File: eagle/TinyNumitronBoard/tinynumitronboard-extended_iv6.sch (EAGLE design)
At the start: 35 parts

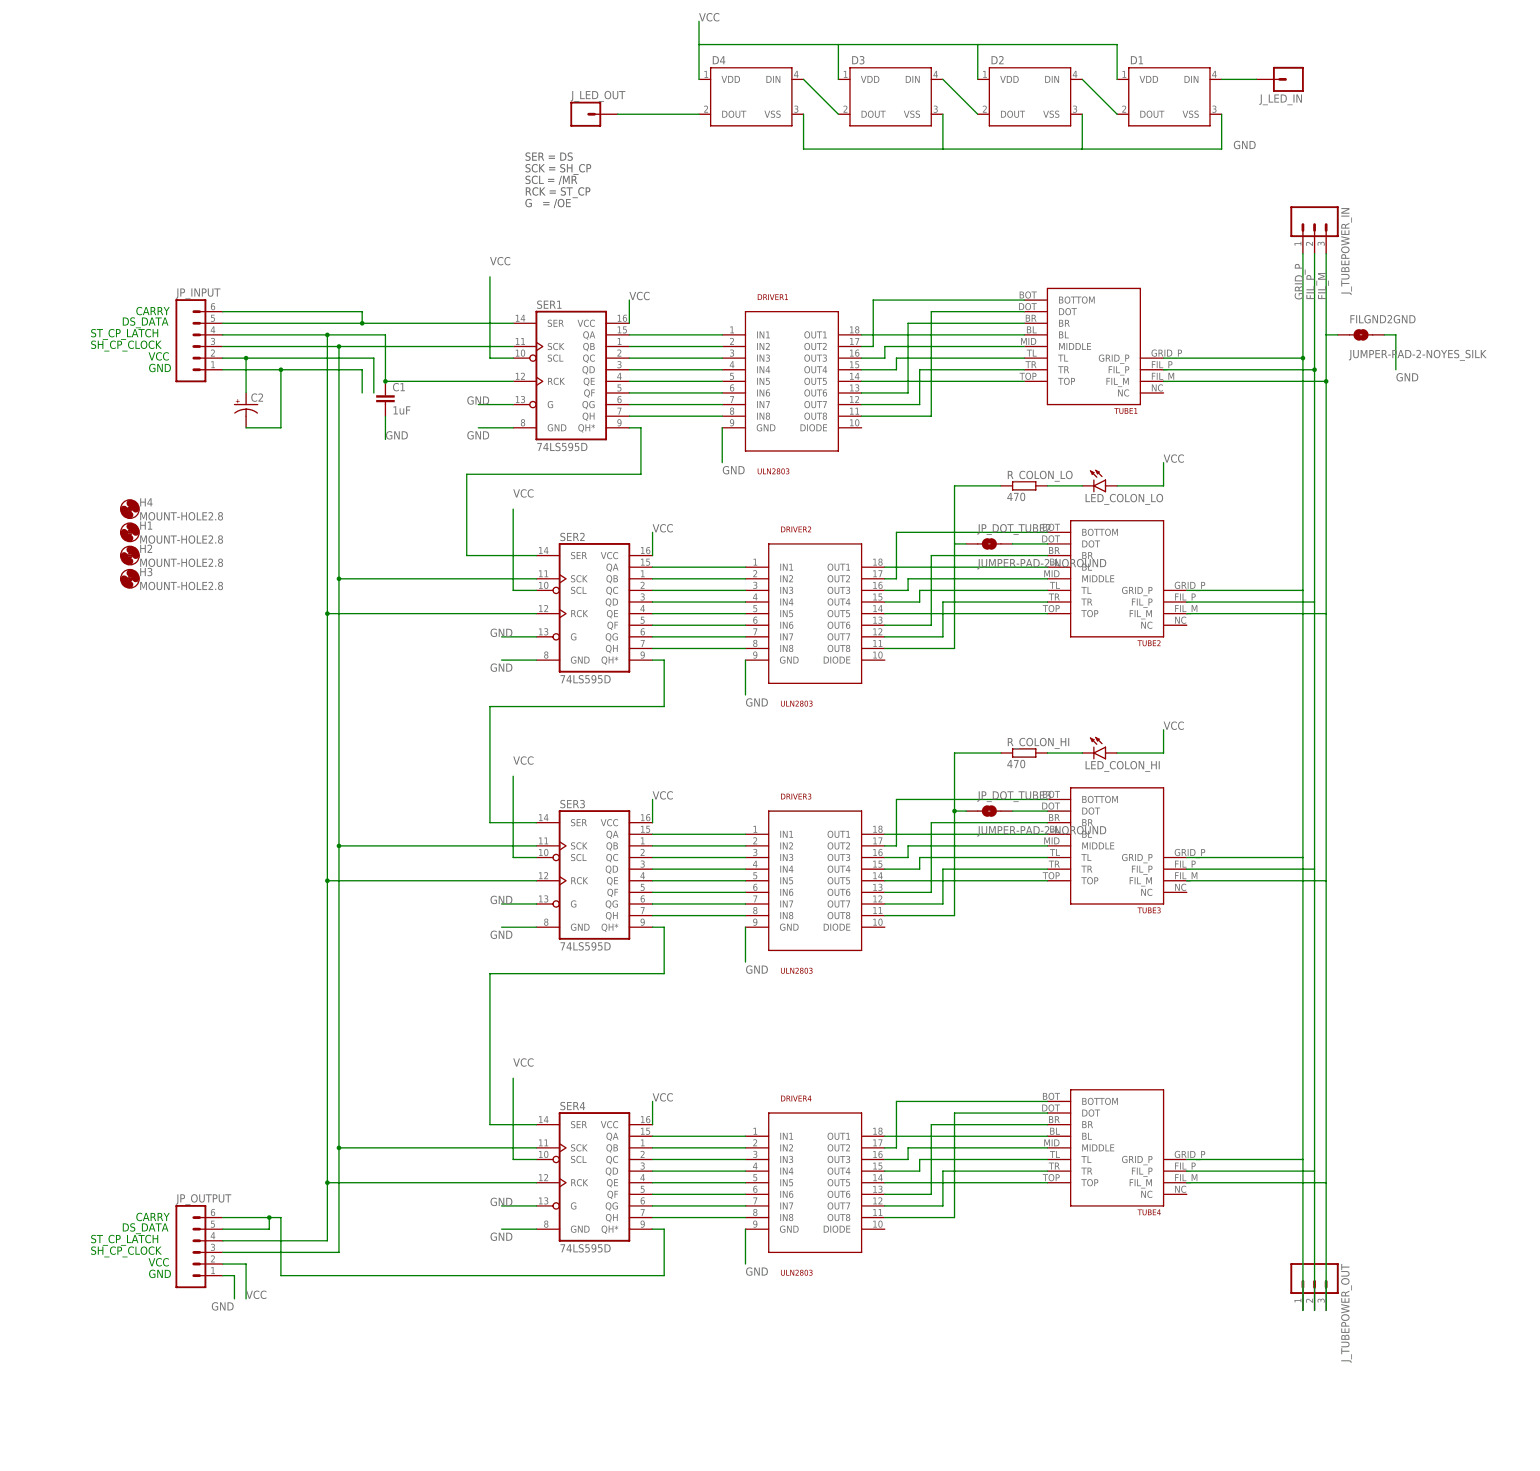
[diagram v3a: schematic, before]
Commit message: added pad for UL2803 diode/common
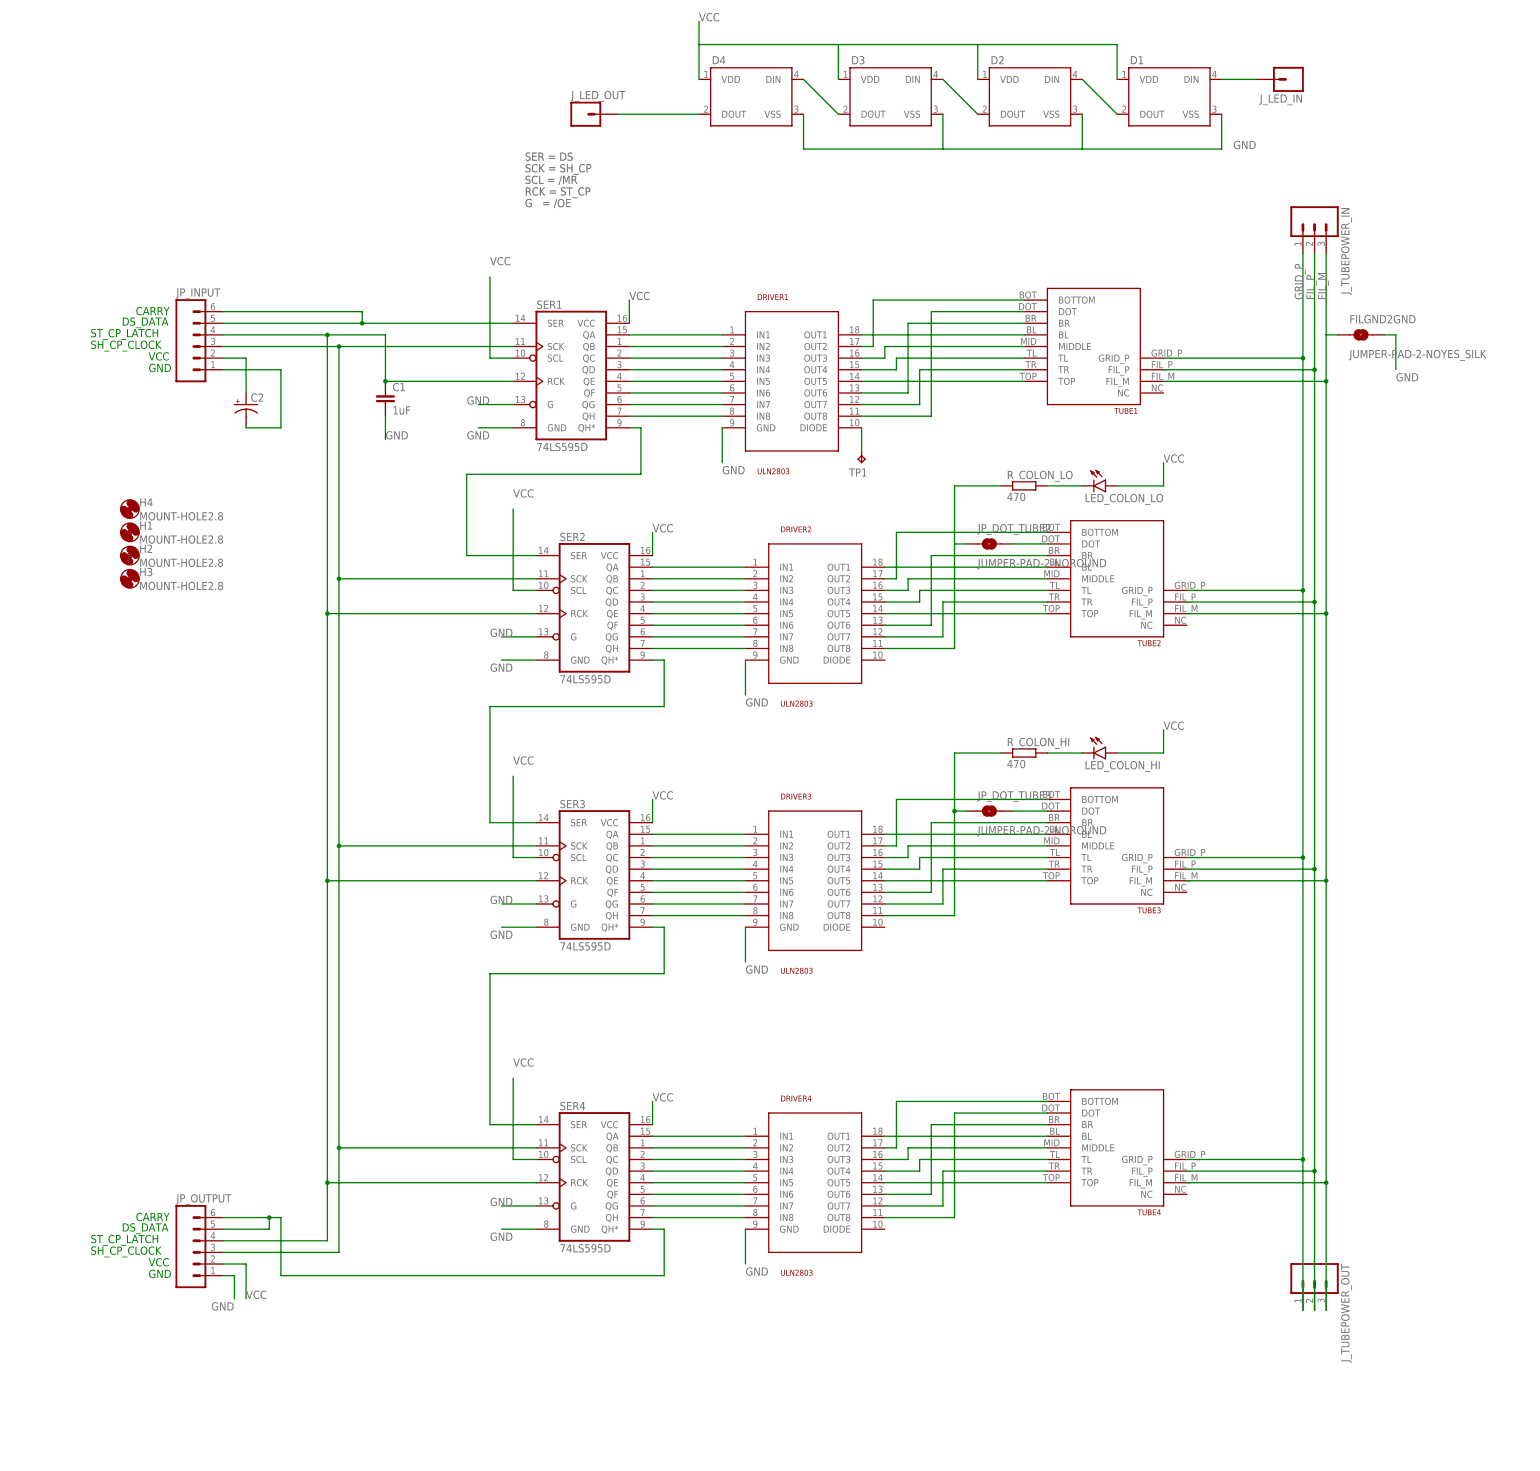
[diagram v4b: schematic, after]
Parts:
- added TP1: TPB2,54, testpad:TPB2,54
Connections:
- new net DIODE: DRIVER1.DIODE, TP1.TP
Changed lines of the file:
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@@
 <part name="R_COLON_HI" library="resistor" deviceset="R-EU_" device="M1206" value="470"/>
 <part name="JP_DOT_TUBE3" library="SparkFun-Passives" deviceset="JUMPER-PAD-2-NO" device="ROUND"/>
+<part name="TP1" library="testpad" deviceset="TP" device="B2,54" value="TPB2,54"/>
 </parts>
 <sheets>
@@
 <instance part="R_COLON_HI" gate="G$1" x="50.8" y="-30.48"/>
 <instance part="JP_DOT_TUBE3" gate="G$1" x="43.18" y="-43.18"/>
+<instance part="TP1" gate="G$1" x="15.24" y="33.02" rot="R180"/>
 </instances>
 <busses>
@@
 <pinref part="JP_INPUT" gate="G$1" pin="2"/>
 <wire x1="-124.46" y1="55.88" x2="-119.38" y2="55.88" width="0.1524" layer="91"/>
-<wire x1="-119.38" y1="55.88" x2="-91.44" y2="55.88" width="0.1524" layer="91"/>
-<wire x1="-91.44" y1="55.88" x2="-91.44" y2="48.26" width="0.1524" layer="91"/>
 <pinref part="C2" gate="G$1" pin="+"/>
 <wire x1="-119.38" y1="48.26" x2="-119.38" y2="55.88" width="0.1524" layer="91"/>
-<junction x="-119.38" y="55.88"/>
 </segment>
 <segment>
@@
 <pinref part="JP_INPUT" gate="G$1" pin="1"/>
 <wire x1="-124.46" y1="53.34" x2="-111.76" y2="53.34" width="0.1524" layer="91"/>
-<wire x1="-111.76" y1="53.34" x2="-93.98" y2="53.34" width="0.1524" layer="91"/>
-<wire x1="-93.98" y1="53.34" x2="-93.98" y2="48.26" width="0.1524" layer="91"/>
 <pinref part="C2" gate="G$1" pin="-"/>
 <wire x1="-119.38" y1="40.64" x2="-111.76" y2="40.64" width="0.1524" layer="91"/>
 <wire x1="-111.76" y1="40.64" x2="-111.76" y2="53.34" width="0.1524" layer="91"/>
-<junction x="-111.76" y="53.34"/>
 </segment>
 <segment>
@@
 <wire x1="86.36" y1="-119.38" x2="111.76" y2="-119.38" width="0.1524" layer="91"/>
 <label x="111.76" y="68.58" size="1.778" layer="95" rot="R90"/>
+<junction x="111.76" y="5.08"/>
+<junction x="111.76" y="-53.34"/>
+<junction x="111.76" y="-119.38"/>
 </segment>
 </net>
@@
 <wire x1="86.36" y1="-121.92" x2="114.3" y2="-121.92" width="0.1524" layer="91"/>
 <label x="114.3" y="68.58" size="1.778" layer="95" rot="R90"/>
+<junction x="114.3" y="2.54"/>
+<junction x="114.3" y="-55.88"/>
+<junction x="114.3" y="-121.92"/>
 </segment>
 </net>
@@
 <pinref part="FILGND2GND" gate="G$1" pin="1"/>
 <wire x1="119.38" y1="60.96" x2="116.84" y2="60.96" width="0.1524" layer="91"/>
+<junction x="116.84" y="0"/>
+<junction x="116.84" y="-58.42"/>
+<junction x="116.84" y="-124.46"/>
 </segment>
 </net>
@@
 </segment>
 </net>
+<net name="DIODE" class="0">
+<segment>
+<pinref part="DRIVER1" gate="G$1" pin="DIODE"/>
+<pinref part="TP1" gate="G$1" pin="TP"/>
+<wire x1="15.24" y1="40.64" x2="15.24" y2="35.56" width="0.1524" layer="91"/>
+</segment>
+</net>

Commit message: Still optimizing/reviewing
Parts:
- JP_DOT_TUBE2, JP_DOT_TUBE3: value JUMPER-PAD-2-NOROUND -> JUMPER-PAD-2-NOYES_SILK; device SparkFun-Passives:JUMPER-PAD-2-NOROUND -> SparkFun-Passives:JUMPER-PAD-2-NOYES_SILK
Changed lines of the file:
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@@
 <part name="LED_COLON_LO" library="SparkFun-LED" deviceset="LED" device="1206"/>
 <part name="R_COLON_LO" library="resistor" deviceset="R-EU_" device="M1206" value="470"/>
-<part name="JP_DOT_TUBE2" library="SparkFun-Passives" deviceset="JUMPER-PAD-2-NO" device="ROUND"/>
+<part name="JP_DOT_TUBE2" library="SparkFun-Passives" deviceset="JUMPER-PAD-2-NO" device="YES_SILK" value="JUMPER-PAD-2-NOYES_SILK"/>
 <part name="LED_COLON_HI" library="SparkFun-LED" deviceset="LED" device="1206"/>
 <part name="R_COLON_HI" library="resistor" deviceset="R-EU_" device="M1206" value="470"/>
-<part name="JP_DOT_TUBE3" library="SparkFun-Passives" deviceset="JUMPER-PAD-2-NO" device="ROUND"/>
+<part name="JP_DOT_TUBE3" library="SparkFun-Passives" deviceset="JUMPER-PAD-2-NO" device="YES_SILK" value="JUMPER-PAD-2-NOYES_SILK"/>
 <part name="TP1" library="testpad" deviceset="TP" device="B2,54" value="TPB2,54"/>
 </parts>

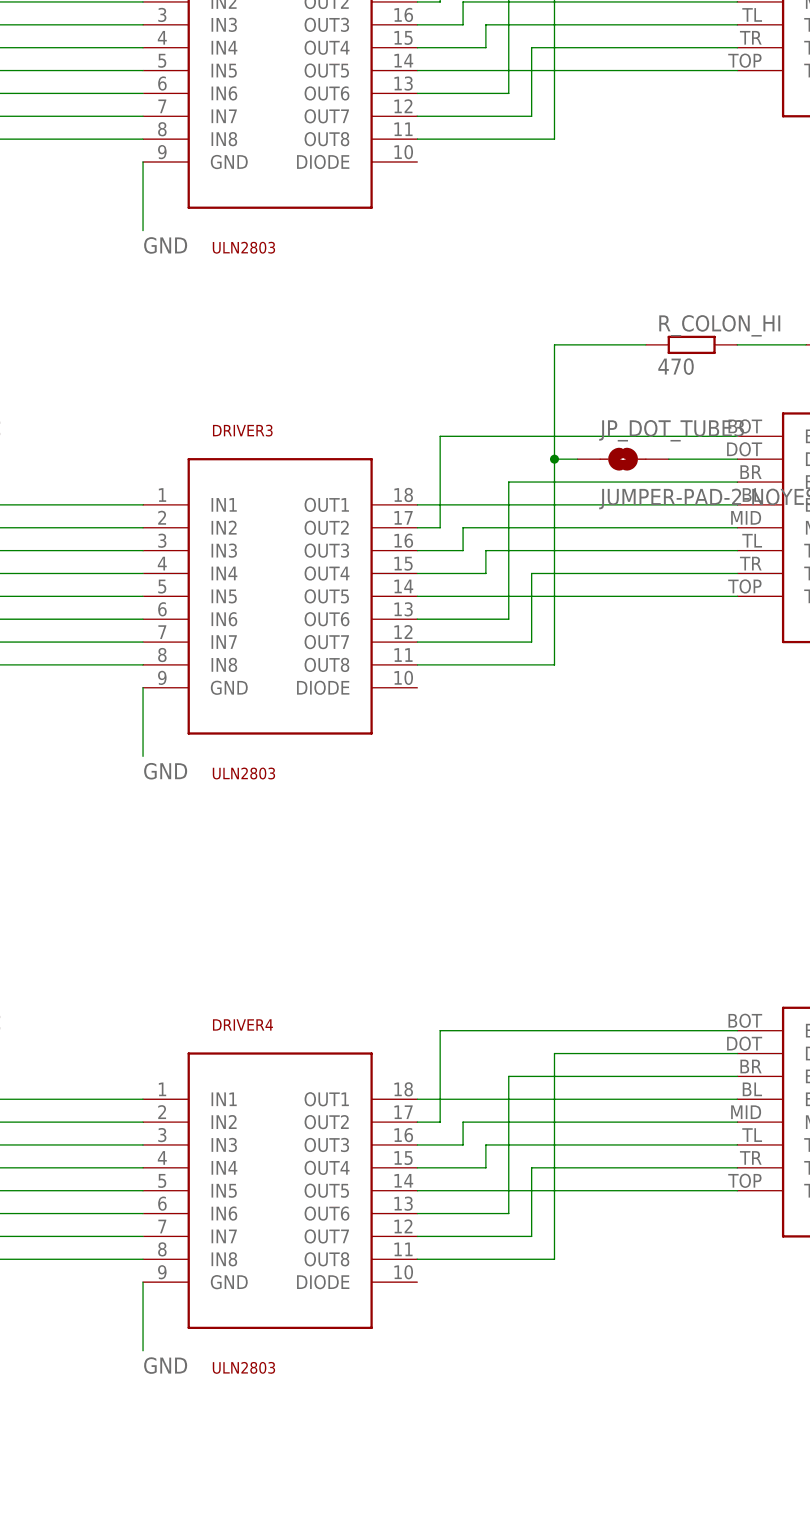
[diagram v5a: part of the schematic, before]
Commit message: Update continued
Labels and additional test points
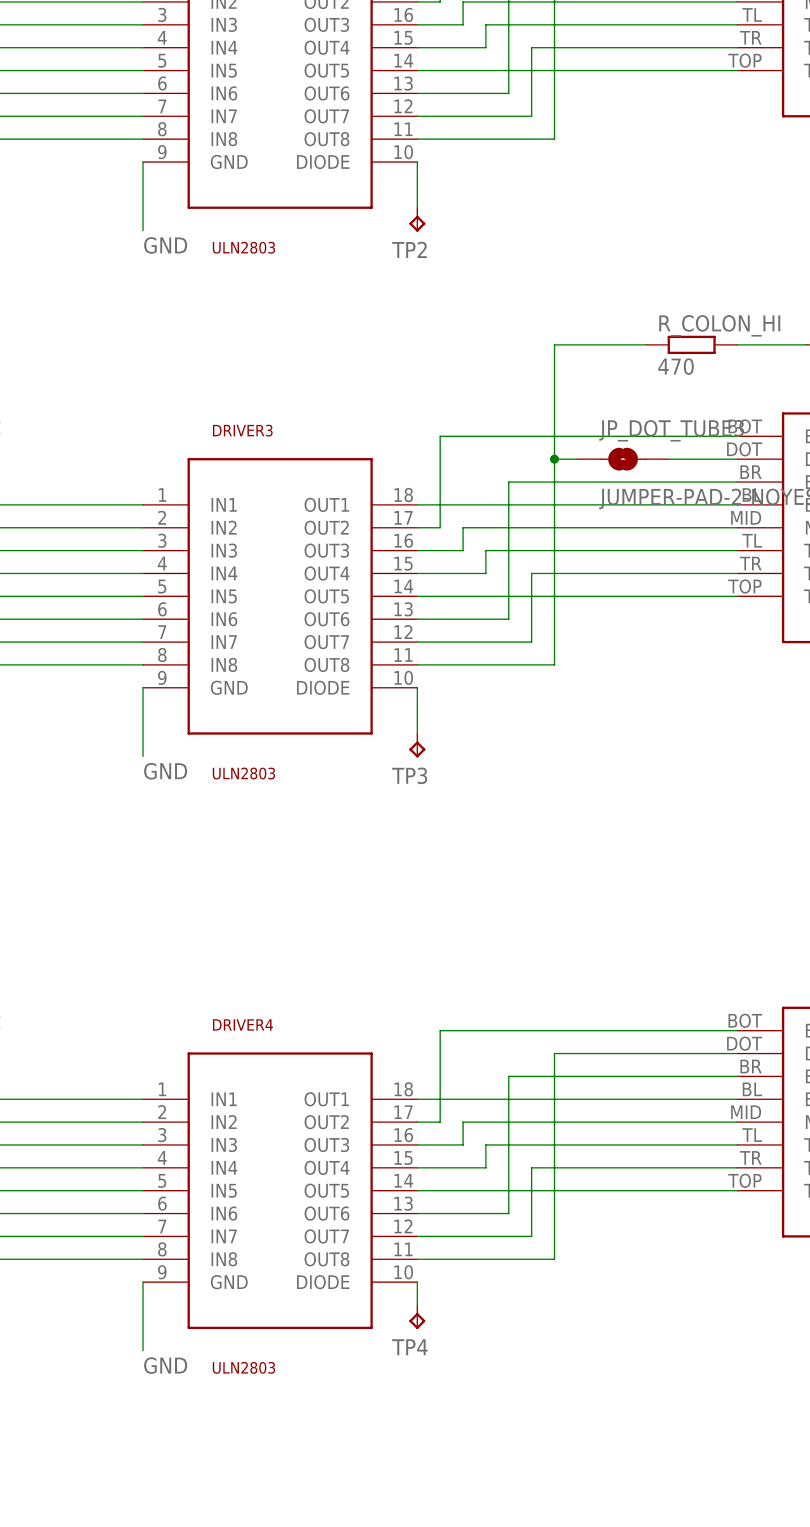
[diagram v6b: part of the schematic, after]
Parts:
- added TP2, TP3, TP4: TPB2,54, testpad:TPB2,54
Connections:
- net DIODE: now also DRIVER2.DIODE, DRIVER3.DIODE, DRIVER4.DIODE, TP2.TP, TP3.TP, TP4.TP
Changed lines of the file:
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@@
 <part name="JP_DOT_TUBE3" library="SparkFun-Passives" deviceset="JUMPER-PAD-2-NO" device="YES_SILK" value="JUMPER-PAD-2-NOYES_SILK"/>
 <part name="TP1" library="testpad" deviceset="TP" device="B2,54" value="TPB2,54"/>
+<part name="TP2" library="testpad" deviceset="TP" device="B2,54" value="TPB2,54"/>
+<part name="TP3" library="testpad" deviceset="TP" device="B2,54" value="TPB2,54"/>
+<part name="TP4" library="testpad" deviceset="TP" device="B2,54" value="TPB2,54"/>
 </parts>
 <sheets>
@@
 <instance part="JP_DOT_TUBE3" gate="G$1" x="43.18" y="-43.18"/>
 <instance part="TP1" gate="G$1" x="15.24" y="33.02" rot="R180"/>
+<instance part="TP2" gate="G$1" x="20.32" y="-17.78" rot="R180"/>
+<instance part="TP3" gate="G$1" x="20.32" y="-76.2" rot="R180"/>
+<instance part="TP4" gate="G$1" x="20.32" y="-139.7" rot="R180"/>
 </instances>
 <busses>
@@
 <wire x1="15.24" y1="40.64" x2="15.24" y2="35.56" width="0.1524" layer="91"/>
 </segment>
-</net>
+<segment>
+<pinref part="DRIVER2" gate="G$1" pin="DIODE"/>
+<pinref part="TP2" gate="G$1" pin="TP"/>
+<wire x1="20.32" y1="-10.16" x2="20.32" y2="-15.24" width="0.1524" layer="91"/>
+</segment>
+<segment>
+<pinref part="DRIVER3" gate="G$1" pin="DIODE"/>
+<pinref part="TP3" gate="G$1" pin="TP"/>
+<wire x1="20.32" y1="-68.58" x2="20.32" y2="-73.66" width="0.1524" layer="91"/>
+</segment>
+<segment>
+<pinref part="DRIVER4" gate="G$1" pin="DIODE"/>
+<pinref part="TP4" gate="G$1" pin="TP"/>
+<wire x1="20.32" y1="-134.62" x2="20.32" y2="-137.16" width="0.1524" layer="91"/>
+</segment>
+</net>
